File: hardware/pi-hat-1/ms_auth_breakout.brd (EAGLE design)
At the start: 65.5 x 57.8 mm, 28 parts, among them IC1 ULN2003AD, J11 BUCK_MODULEHORIZONTAL, J9 POWER_JACKPTH_LOCK, Q1 DMN3023L, Q2 DMN3023L, Q3 DMN3023L, Q4 DMN3023L

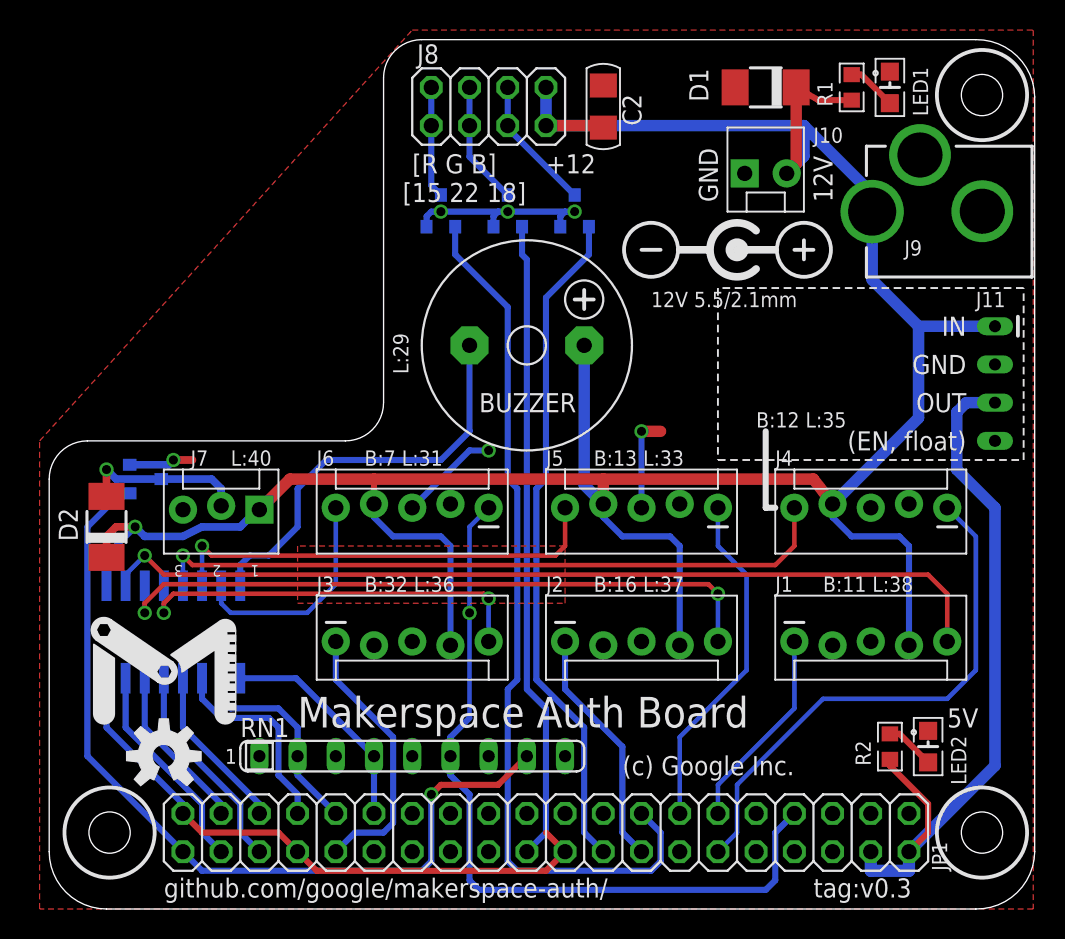
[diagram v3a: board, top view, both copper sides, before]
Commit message: Reroute +12 line to avoid ground island
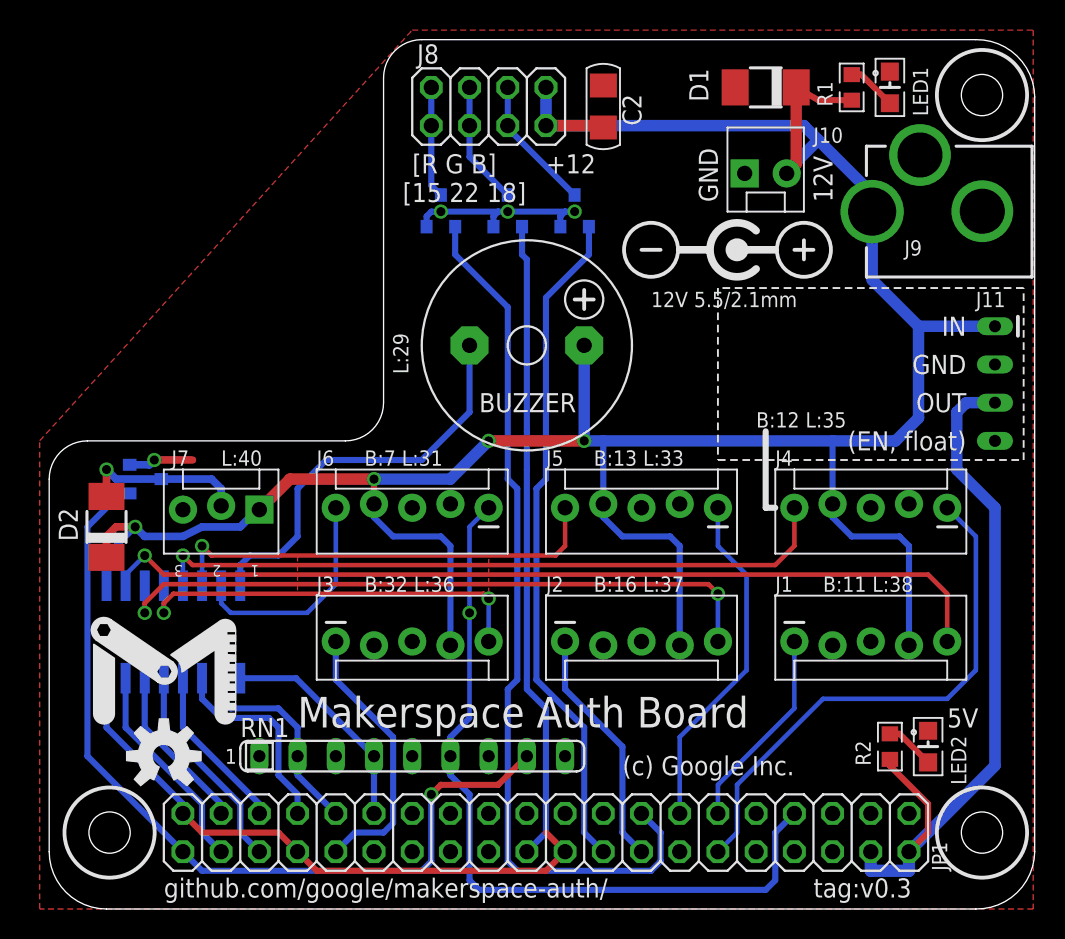
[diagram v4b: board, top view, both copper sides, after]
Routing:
- net GND: track 70.6 -> 57.6 mm, vias 6 -> 4
- net +12V: vias 1 -> 4
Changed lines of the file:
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@@
 <wire x1="48.895" y1="26.67" x2="49.53" y2="26.67" width="0.4064" layer="21"/>
 <text x="25.146" y="35.56" size="1.016" layer="21" ratio="20" rot="R90">L:29</text>
-<text x="13.335" y="29.464" size="1.016" layer="21" ratio="20">L:40</text>
+<text x="12.7" y="29.464" size="1.016" layer="21" ratio="20">L:40</text>
 <text x="62.865" y="40.005" size="1.016" layer="25" ratio="12">J11</text>
 </plain>
@@
 <attribute name="SF_ID" value="PRT-08096" x="15.24" y="26.67" size="1.778" layer="27" rot="R180" display="off"/>
 <attribute name="PROD_ID" value="CONN-08625" x="15.24" y="26.67" size="1.778" layer="27" rot="R180" display="off"/>
-<attribute name="NAME" x="10.668" y="29.464" size="1.016" layer="25" font="vector" ratio="20"/>
+<attribute name="NAME" x="9.398" y="29.464" size="1.016" layer="25" font="vector" ratio="20"/>
 <attribute name="VALUE" x="14.351" y="29.464" size="0.6096" layer="27" font="vector" ratio="20" rot="R180" align="top-left"/>
 </element>
@@
 <via x="31.75" y="46.355" extent="1-16" drill="0.6"/>
 <via x="36.195" y="46.355" extent="1-16" drill="0.6"/>
-<wire x1="6.62" y1="29.525" x2="9.205" y2="29.525" width="0.508" layer="16"/>
-<wire x1="9.205" y1="29.525" x2="9.525" y2="29.845" width="0.508" layer="16"/>
-<via x="9.525" y="29.845" extent="1-16" drill="0.6"/>
-<wire x1="9.525" y1="29.845" x2="10.795" y2="29.845" width="0.508" layer="1"/>
+<wire x1="6.62" y1="29.525" x2="7.935" y2="29.525" width="0.508" layer="16"/>
+<wire x1="7.935" y1="29.525" x2="8.255" y2="29.845" width="0.508" layer="16"/>
+<via x="8.255" y="29.845" extent="1-16" drill="0.6"/>
+<wire x1="8.255" y1="29.845" x2="10.795" y2="29.845" width="0.508" layer="1"/>
 <contactref element="RN1" pad="5"/>
 <contactref element="RN1" pad="3"/>
@@
 <wire x1="5.08" y1="12.065" x2="10.16" y2="6.985" width="0.4064" layer="16"/>
 <wire x1="10.16" y1="6.985" x2="10.16" y2="6.35" width="0.4064" layer="16"/>
-<wire x1="40.64" y1="26.67" x2="40.64" y2="31.75" width="0.4064" layer="16"/>
-<via x="40.64" y="31.75" extent="1-16" drill="0.6"/>
-<wire x1="40.64" y1="31.75" x2="41.91" y2="31.75" width="0.762" layer="1"/>
-<wire x1="25.4" y1="26.67" x2="29.21" y2="30.48" width="0.4064" layer="16"/>
-<via x="30.48" y="30.48" extent="1-16" drill="0.6"/>
-<wire x1="29.21" y1="30.48" x2="30.48" y2="30.48" width="0.4064" layer="16"/>
 </signal>
 <signal name="TXD">
@@
 <contactref element="J8" pad="8"/>
 <contactref element="J8" pad="7"/>
-<wire x1="52.07" y1="28.575" x2="38.1" y2="28.575" width="0.762" layer="1"/>
-<wire x1="38.1" y1="28.575" x2="22.86" y2="28.575" width="0.762" layer="1"/>
 <wire x1="22.86" y1="28.575" x2="17.272" y2="28.575" width="0.762" layer="1"/>
 <wire x1="34.29" y1="54.61" x2="34.29" y2="52.07" width="0.762" layer="16"/>
 <wire x1="34.29" y1="52.07" x2="51.435" y2="52.07" width="0.762" layer="16"/>
-<wire x1="51.435" y1="52.07" x2="55.88" y2="47.625" width="0.762" layer="16"/>
+<wire x1="51.435" y1="52.07" x2="52.3875" y2="51.1175" width="0.762" layer="16"/>
+<wire x1="52.3875" y1="51.1175" x2="55.88" y2="47.625" width="0.762" layer="16"/>
 <wire x1="55.88" y1="47.625" x2="55.88" y2="46.4472" width="0.762" layer="16"/>
 <wire x1="55.88" y1="46.4472" x2="55.9722" y2="46.355" width="0.762" layer="16"/>
-<wire x1="51.435" y1="52.07" x2="51.435" y2="50.038" width="0.762" layer="16"/>
-<wire x1="51.435" y1="50.038" x2="50.292" y2="48.895" width="0.762" layer="16"/>
 <wire x1="50.92" y1="54.61" x2="50.92" y2="49.523" width="0.762" layer="1"/>
 <wire x1="50.92" y1="49.523" x2="50.292" y2="48.895" width="0.762" layer="1"/>
 <wire x1="54.61" y1="53.76" x2="52.405" y2="53.76" width="0.4064" layer="1"/>
 <wire x1="52.405" y1="53.76" x2="50.92" y2="54.61" width="0.4064" layer="1"/>
-<wire x1="53.34" y1="26.924" x2="52.07" y2="28.575" width="0.762" layer="1"/>
 <wire x1="55.9722" y1="46.355" x2="55.9722" y2="41.8178" width="0.762" layer="16"/>
 <wire x1="55.9722" y1="41.8178" x2="59.055" y2="38.735" width="0.762" layer="16"/>
 <wire x1="59.055" y1="38.735" x2="64.135" y2="38.735" width="0.762" layer="16"/>
 <wire x1="59.055" y1="38.735" x2="59.055" y2="32.639" width="0.762" layer="16"/>
-<wire x1="59.055" y1="32.639" x2="53.34" y2="26.924" width="0.762" layer="16"/>
 <wire x1="17.272" y1="28.575" x2="15.24" y2="26.543" width="0.762" layer="1"/>
-<wire x1="38.1" y1="26.924" x2="38.1" y2="28.575" width="0.762" layer="1"/>
-<wire x1="36.83" y1="37.465" x2="36.83" y2="28.194" width="0.762" layer="16"/>
-<wire x1="36.83" y1="28.194" x2="38.1" y2="26.924" width="0.762" layer="16"/>
+<wire x1="36.83" y1="37.465" x2="36.83" y2="31.115" width="0.762" layer="16"/>
 <wire x1="53.34" y1="26.924" x2="53.34" y2="26.035" width="0.4064" layer="16"/>
 <wire x1="53.34" y1="26.035" x2="54.61" y2="24.765" width="0.4064" layer="16"/>
@@
 <wire x1="6.985" y1="25.4" x2="5.08" y2="23.495" width="0.4064" layer="16"/>
 <wire x1="7.62" y1="24.765" x2="6.985" y2="25.4" width="0.508" layer="16"/>
+<wire x1="22.86" y1="28.575" x2="27.94" y2="28.575" width="0.762" layer="16"/>
+<wire x1="27.94" y1="28.575" x2="30.48" y2="31.115" width="0.762" layer="16"/>
+<wire x1="30.48" y1="31.115" x2="36.83" y2="31.115" width="0.762" layer="1"/>
+<via x="36.83" y="31.115" extent="1-16" drill="0.6"/>
+<via x="30.48" y="31.115" extent="1-16" drill="0.6"/>
+<via x="22.86" y="28.575" extent="1-16" drill="0.6"/>
+<wire x1="36.83" y1="31.115" x2="38.1" y2="31.115" width="0.762" layer="16"/>
+<wire x1="38.1" y1="31.115" x2="53.34" y2="31.115" width="0.762" layer="16"/>
+<wire x1="53.34" y1="31.115" x2="57.531" y2="31.115" width="0.762" layer="16"/>
+<wire x1="57.531" y1="31.115" x2="59.055" y2="32.639" width="0.762" layer="16"/>
+<wire x1="53.34" y1="26.924" x2="53.34" y2="31.115" width="0.4064" layer="16"/>
+<wire x1="38.1" y1="26.924" x2="38.1" y2="31.115" width="0.4064" layer="16"/>
+<wire x1="50.292" y1="48.895" x2="50.292" y2="49.022" width="0.762" layer="16"/>
+<wire x1="50.292" y1="49.022" x2="52.3875" y2="51.1175" width="0.762" layer="16"/>
 </signal>
 <signal name="L5_LOGIC">
@@
 <wire x1="28.255" y1="45.355" x2="28.255" y2="43.5" width="0.4064" layer="16"/>
 <wire x1="32.385" y1="27.94" x2="32.385" y2="15.24" width="0.4064" layer="16"/>
-<wire x1="31.75" y1="28.575" x2="31.75" y2="40.005" width="0.4064" layer="16"/>
 <wire x1="31.75" y1="40.005" x2="28.255" y2="43.5" width="0.4064" layer="16"/>
 <contactref element="JP1" pad="15"/>
@@
 <wire x1="32.385" y1="15.24" x2="31.75" y2="14.605" width="0.4064" layer="16"/>
 <wire x1="31.75" y1="14.605" x2="31.75" y2="3.175" width="0.4064" layer="16"/>
+<wire x1="31.75" y1="40.005" x2="31.75" y2="28.575" width="0.4064" layer="16"/>
 </signal>
 <signal name="G_LOGIC">
@@
 <wire x1="34.29" y1="5.08" x2="34.29" y2="13.335" width="0.4064" layer="16"/>
 <wire x1="34.29" y1="13.335" x2="33.02" y2="14.605" width="0.4064" layer="16"/>
-<wire x1="33.02" y1="14.605" x2="33.02" y2="43.175" width="0.4064" layer="16"/>
+<wire x1="33.02" y1="14.605" x2="33.02" y2="29.21" width="0.4064" layer="16"/>
+<wire x1="33.02" y1="29.21" x2="33.02" y2="31.75" width="0.4064" layer="16"/>
+<wire x1="33.02" y1="31.75" x2="33.02" y2="43.175" width="0.4064" layer="16"/>
 </signal>
 <signal name="B_LOGIC">
@@
 <wire x1="37.145" y1="45.355" x2="37.145" y2="43.495" width="0.4064" layer="16"/>
 <wire x1="33.655" y1="27.94" x2="33.655" y2="15.24" width="0.4064" layer="16"/>
-<wire x1="34.29" y1="28.575" x2="34.29" y2="40.64" width="0.4064" layer="16"/>
+<contactref element="JP1" pad="18"/>
 <wire x1="34.29" y1="40.64" x2="37.145" y2="43.495" width="0.4064" layer="16"/>
-<contactref element="JP1" pad="18"/>
 <wire x1="36.83" y1="5.08" x2="38.1" y2="3.81" width="0.4064" layer="16"/>
 <wire x1="36.83" y1="12.065" x2="33.655" y2="15.24" width="0.4064" layer="16"/>
 <wire x1="36.83" y1="12.065" x2="36.83" y2="5.08" width="0.4064" layer="16"/>
+<wire x1="34.29" y1="28.575" x2="34.29" y2="40.64" width="0.4064" layer="16"/>
 </signal>
 <signal name="!R">
@@
 <contactref element="IC1" pad="16"/>
 <contactref element="BUZZER" pad="-"/>
-<wire x1="19.685" y1="29.845" x2="27.305" y2="29.845" width="0.4064" layer="16"/>
-<wire x1="27.305" y1="29.845" x2="29.21" y2="31.75" width="0.4064" layer="16"/>
-<wire x1="29.21" y1="31.75" x2="29.21" y2="37.465" width="0.4064" layer="16"/>
-<wire x1="15.875" y1="23.495" x2="17.78" y2="25.4" width="0.4064" layer="16"/>
-<wire x1="17.78" y1="25.4" x2="17.78" y2="27.94" width="0.4064" layer="16"/>
-<wire x1="17.78" y1="27.94" x2="19.685" y2="29.845" width="0.4064" layer="16"/>
-<wire x1="15.875" y1="23.495" x2="14.605" y2="23.495" width="0.4064" layer="16"/>
+<wire x1="19.685" y1="29.845" x2="26.035" y2="29.845" width="0.4064" layer="16"/>
+<wire x1="26.035" y1="29.845" x2="29.21" y2="33.02" width="0.4064" layer="16"/>
+<wire x1="29.21" y1="33.02" x2="29.21" y2="37.465" width="0.4064" layer="16"/>
 <wire x1="14.605" y1="23.495" x2="13.97" y2="22.86" width="0.4064" layer="16"/>
 <wire x1="13.97" y1="22.86" x2="13.97" y2="21.4884" width="0.4064" layer="16"/>
+<wire x1="19.685" y1="29.845" x2="17.78" y2="27.94" width="0.4064" layer="16"/>
+<wire x1="17.78" y1="27.94" x2="17.78" y2="24.765" width="0.4064" layer="16"/>
+<wire x1="17.78" y1="24.765" x2="16.51" y2="23.495" width="0.4064" layer="16"/>
+<wire x1="16.51" y1="23.495" x2="14.605" y2="23.495" width="0.4064" layer="16"/>
 </signal>
 <signal name="B6_LOGIC">
@@
 <signal name="N$1">
 <polygon width="0.3048" layer="1" pour="cutout">
-<vertex x="17.78" y="24.13"/>
-<vertex x="17.78" y="20.32"/>
-<vertex x="35.56" y="20.32"/>
-<vertex x="35.56" y="24.13"/>
+<vertex x="17.78" y="23.495"/>
+<vertex x="17.78" y="20.955"/>
+<vertex x="30.48" y="20.955"/>
+<vertex x="30.48" y="23.495"/>
 </polygon>
 </signal>

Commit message: Rework board to add two relays.
Also remove buzzer, change LED connector, and standardize on smaller
freewheel diodes.  Not quire ready for 0.4 cut; needs airwires routed
for relays with solder jumpers.
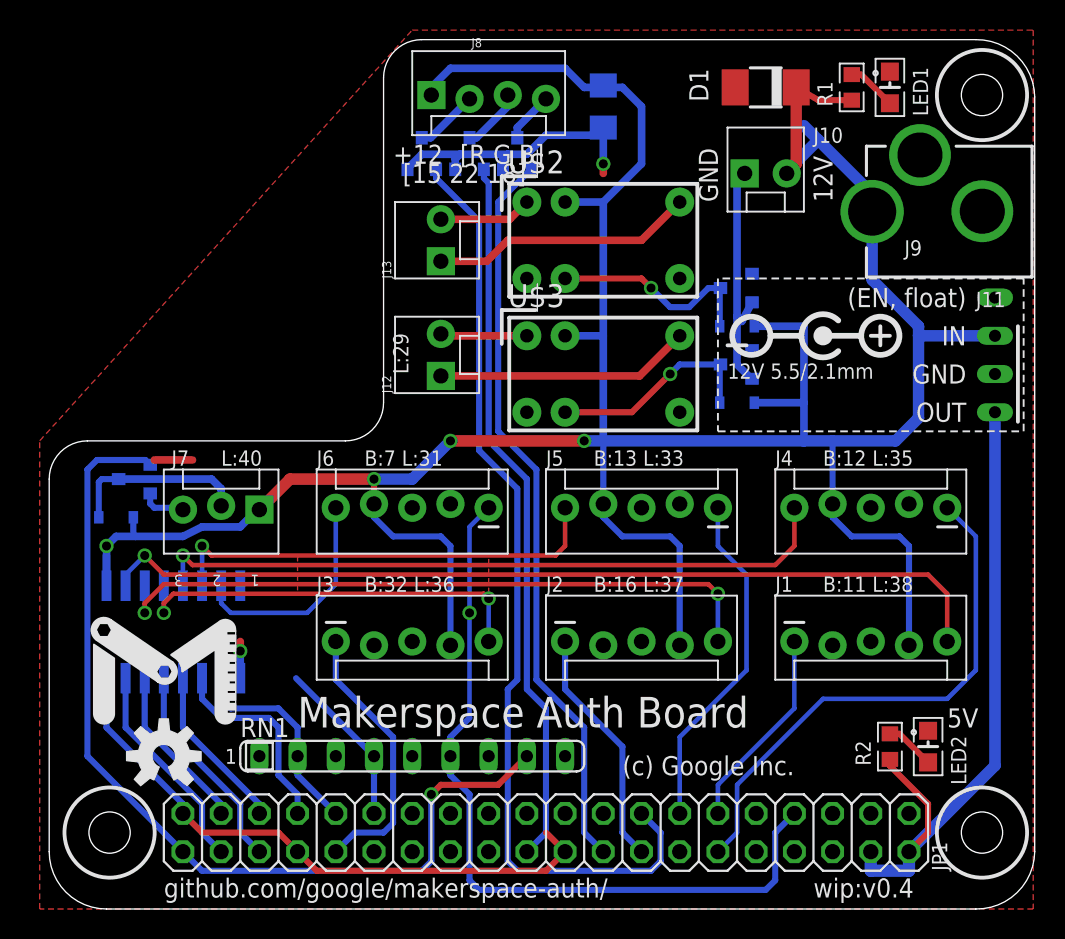
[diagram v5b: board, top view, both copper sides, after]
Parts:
- removed BUZZER: F/CM12P, buzzer:F/CM12P
- added D3, D4: 250mA/100V, SparkFun-DiscreteSemi:SOD-323
- added J12, J13: (no value), SparkFun-Connectors:MOLEX-1X2_LOCK
- added Q5, Q6: DMN3023L, SparkFun-DiscreteSemi:SOT23-3
- added U$2, U$3: HFD23_SPDT, hfd23:HFD23
- D2: value (none) -> 250mA/100V; device diode:DO-214AC -> SparkFun-DiscreteSemi:SOD-323
- J8: device pinhead:2X04 -> SparkFun-Connectors:MOLEX-1X4_LOCK
- moved Q3 5.39 mm to (32.4, 50.2)
- moved Q2 4.58 mm to (29.2, 50.2)
- moved Q1 4.02 mm to (26.0, 50.2)
- moved J8 3.86 mm to (26.7, 54.0)
- moved D2 0.90 mm to (5.71, 26.0), flipped to the bottom, turned to 0 degrees
- moved Q4 0.63 mm to (6.99, 28.6), turned to 270 degrees
- moved J11 0.63 mm to (64.1, 35.6)
- flipped C2 to the bottom, turned to 270 degrees
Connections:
- removed net N$13: BUZZER.-, IC1.16
- new net N$10: J13.1, U$2.3
- new net N$12: J12.1, U$3.3
- new net N$14: J12.2, U$3.1
- new net N$2: D4.A, Q6.3, U$3.5
- new net N$5: D3.A, Q5.3, U$2.5
- new net N$9: J13.2, U$2.1
- new net RELAY_1: Q5.1
- new net RELAY_2: Q6.1
- net !B: now also J8.4; no longer J8.5, J8.6
- net !G: no longer J8.4
- net !R: no longer J8.1
- net +12V: now also D3.C, D4.C, J8.1, U$2.2, U$3.2; no longer BUZZER.+, J8.7, J8.8
- net GND: now also IC1.1, Q5.2, Q6.2
- net L7_LOGIC: no longer IC1.1
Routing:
- net +12V: track 184.4 -> 212.9 mm
- net N$13: track 27.1 -> 0.00 mm
- net GND: track 57.6 -> 84.1 mm, vias 4 -> 2
- net N$10: track 0.00 -> 17.5 mm
- net N$12: track 0.00 -> 17.0 mm
- net N$2: track 0.00 -> 14.2 mm, vias 0 -> 1
- net N$5: track 0.00 -> 14.2 mm, vias 0 -> 1
- net N$9: track 0.00 -> 6.19 mm
- net N$14: track 0.00 -> 5.77 mm
- net !B: track 9.00 -> 3.37 mm
- net G_LOGIC: track 42.7 -> 47.6 mm
- net HC_LOGIC: track 57.1 -> 61.7 mm
- net B_LOGIC: track 44.8 -> 49.2 mm
- net R_LOGIC: track 58.5 -> 62.9 mm
- net !G: track 8.21 -> 4.16 mm
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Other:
- board text added: "wip:v0.4"
- board text removed: "tag:v0.3"

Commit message: pi-hat-1 v0.4 as-ordered
(Forgot to route the relay connections though.)
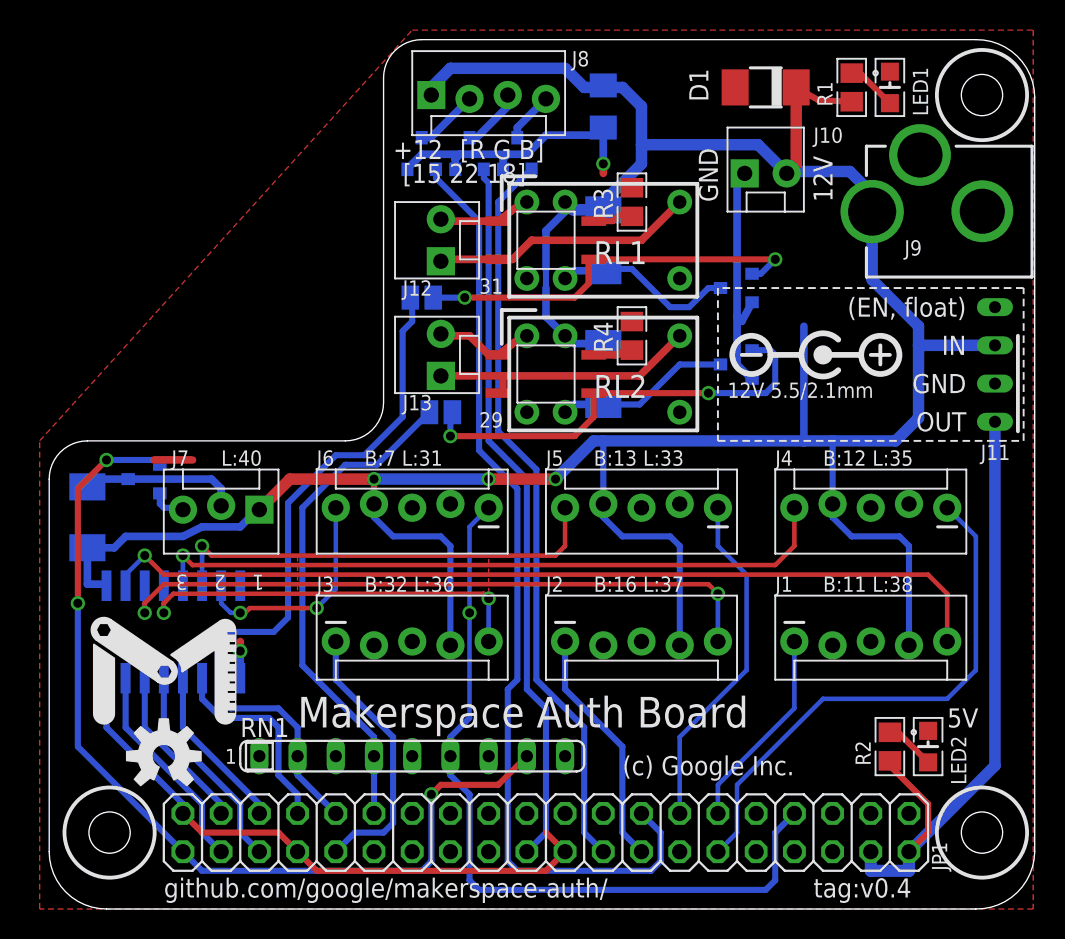
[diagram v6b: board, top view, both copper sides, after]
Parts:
- added IC3, IC4: CPC1017, cpc1017:SOP-4
- added R3, R4: 1k, Tim-Pretty:R0805
- added SJ1, SJ2: (no value), jumper:SJ
- D2, D3, D4: value 250mA/100V -> (none); device SparkFun-DiscreteSemi:SOD-323 -> diode:DO-214AC
- R1, R2: device Tim-Pretty:R0603 -> Tim-Pretty:R0805
- moved D4 43.8 mm to (3.81, 26.0), turned to 90 degrees
- moved D2 33.8 mm to (38.1, 35.6), turned to 270 degrees
- moved D3 10.6 mm to (38.1, 44.5), turned to 270 degrees
- moved J12 7.62 mm to (27.3, 43.2)
- moved J13 7.62 mm to (27.3, 35.6)
- moved J11 0.64 mm to (64.1, 34.9)
- moved Q4 0.63 mm to (7.62, 28.6)
- renumbered U$2 to RL1, U$3 to RL2
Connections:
- removed net N$14: J12.2, RL2.1
- new net N$13: IC4.2, R4.2
- new net N$6: IC3.3, J12.2, RL1.1
- new net N$8: IC3.2, R3.2
- net GND: now also R3.1, R4.1
- net L6_LOGIC: now also SJ1.2
- net L7_LOGIC: now also SJ2.2
- net N$10: now also IC3.4, J12.1; no longer J13.1
- net N$12: now also IC4.4, J13.1; no longer J12.1
- net N$2: now also D2.A; no longer D4.A
- net N$4: now also D4.A; no longer D2.A
- net N$9: now also IC4.3, RL2.1; no longer RL1.1
- net RELAY_1: now also IC3.1, SJ1.1
- net RELAY_2: now also IC4.1, SJ2.1
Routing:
- net L6_LOGIC: track 14.0 -> 47.4 mm
- net RELAY_2: track 0.00 -> 29.2 mm, vias 0 -> 2
- net RELAY_1: track 0.00 -> 26.6 mm, vias 0 -> 2
- net L7_LOGIC: track 11.1 -> 33.4 mm
- net N$6: track 0.00 -> 6.20 mm
- net N$14: track 5.77 -> 0.00 mm
- net +12V: track 212.9 -> 208.1 mm, vias 4 -> 3
- net N$8: track 0.00 -> 2.72 mm
- net N$13: track 0.00 -> 2.59 mm
- net N$2: track 14.2 -> 11.7 mm, vias 1 -> 0
- net N$5: track 14.2 -> 12.2 mm, vias 1 -> 0
- net N$12: track 17.0 -> 18.4 mm
- net HC_LOGIC: track 61.7 -> 62.5 mm, vias 1 -> 3
- net +5V: track 44.4 -> 43.6 mm
- net GND: track 84.1 -> 83.5 mm
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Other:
- board text added: "29"
- board text added: "31"
- board text added: "tag:v0.4"
- board text removed: "L:29"
- board text removed: "wip:v0.4"
